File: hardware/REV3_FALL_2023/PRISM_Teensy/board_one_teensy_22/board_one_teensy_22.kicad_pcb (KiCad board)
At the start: 2 copper layers, 61 x 88.9 mm, 21 parts, among them J1 EAST, J2 CORE_IO, J3 USB_micro, U1 Teensy4.1, U2 BNO055_Breakout, U3 3966

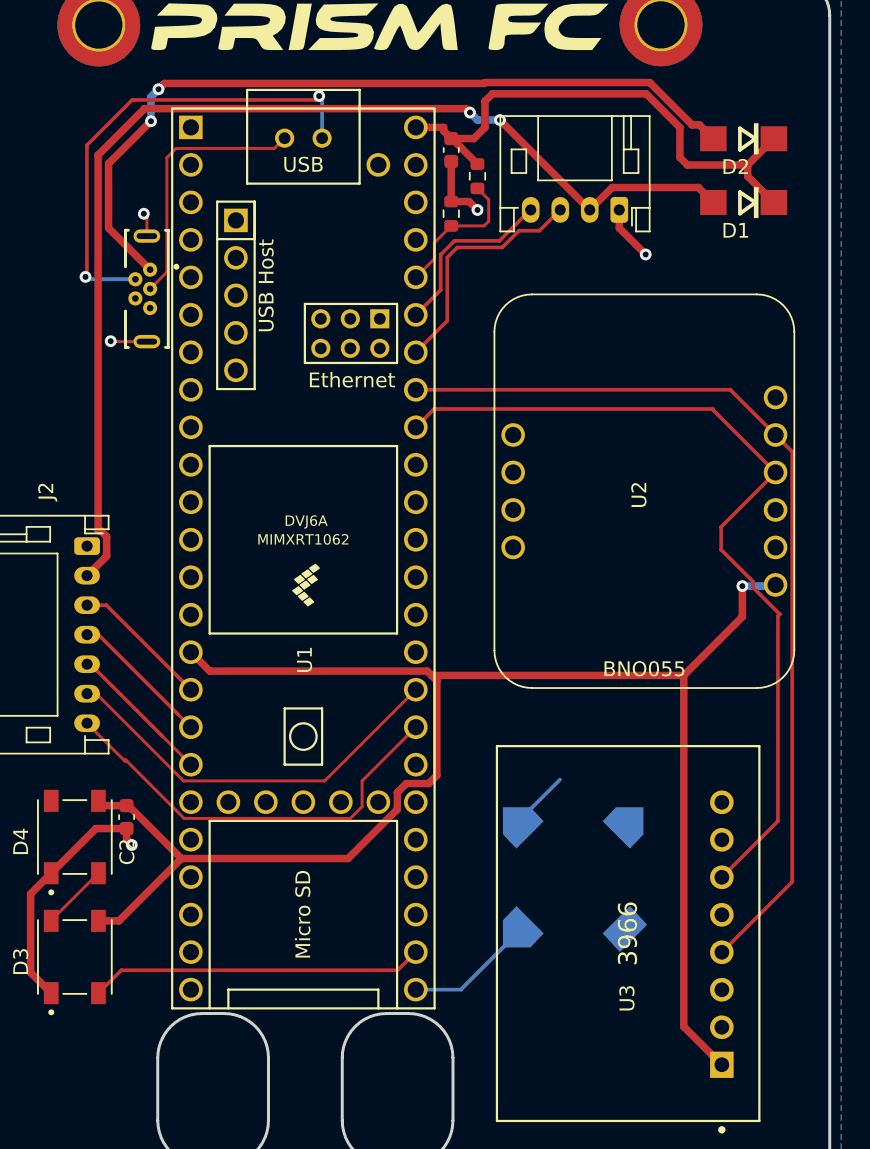
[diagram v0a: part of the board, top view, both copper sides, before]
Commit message: added teensy 4.0 and new connector spec
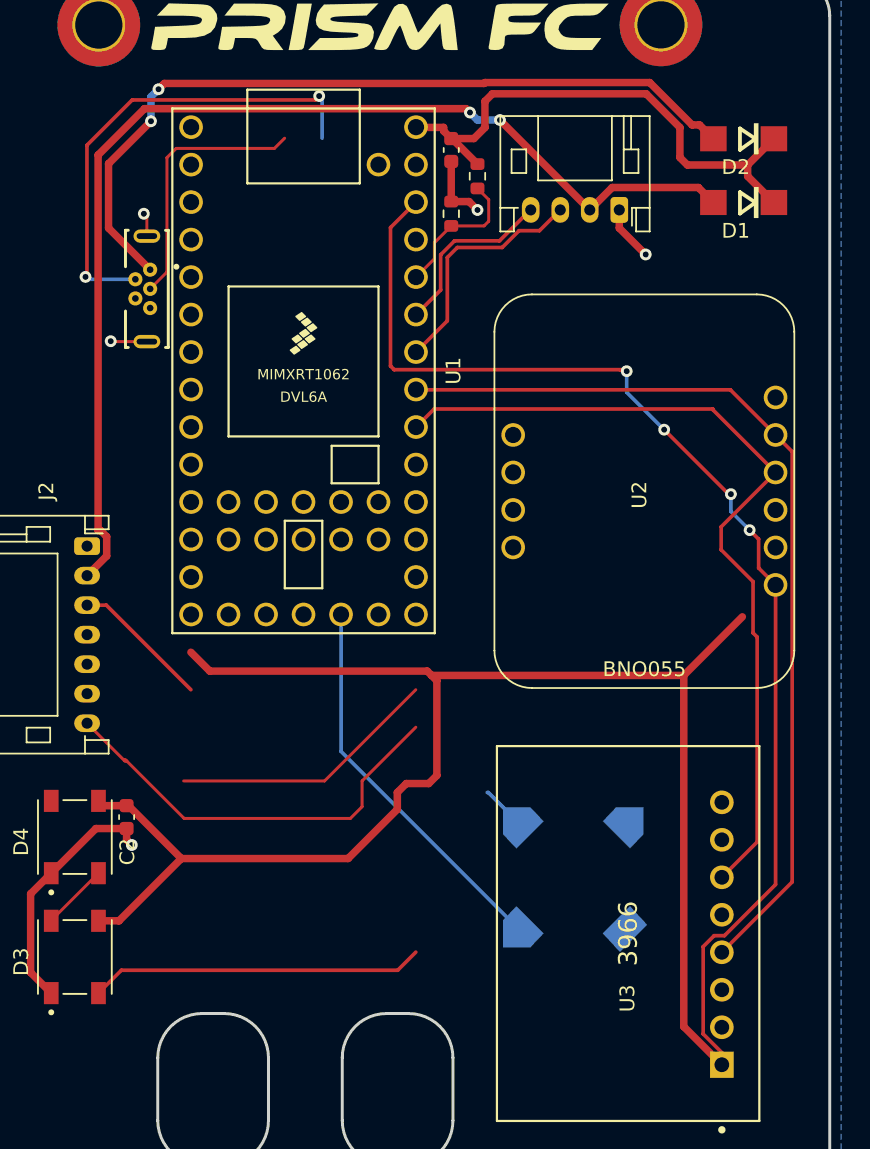
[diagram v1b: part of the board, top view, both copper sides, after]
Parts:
- U1: value Teensy4.1 -> Teensy4.0; footprint Teensy:Teensy41 -> Teensy_4.1:Teensy40
- moved U1 12.7 mm to (132.5, 76.7)
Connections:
- C2 pad 2: /3.3V -> /5V
- D3 pad 3: /3.3V -> /5V
- D4 pad 3: /3.3V -> /5V
- U1 pad 15: /3.3V -> unconnected-(U1-Pad15)
- U1 pad 16: /PYRO 1 -> unconnected-(U1-Pad16)
- U1 pad 17: /PYRO 2 -> unconnected-(U1-Pad17)
- U1 pad 18: /ARM -> /BUZZER
- U1 pad 25: /BUZZER -> /SDA 0
- U1 pad 26: /NEOPIXEL -> /SCL 0
- U1 pad 27: unconnected-(U1-Pad27) -> /CONT 1
- U1 pad 28: unconnected-(U1-Pad28) -> /CONT 2
- U1 pad 31: unconnected-(U1-Pad31) -> /3.3V
- U1 pad 32: /CONT 2 -> GND
- U1 pad 33: /CONT 1 -> /5V
- U1 pad 35: unconnected-(U1-Pad35) -> /PYRO 1
- U1 pad 36: unconnected-(U1-Pad36) -> /PYRO 2
- U1 pad 37: unconnected-(U1-Pad37) -> /ARM
- U1 pad 38: unconnected-(U1-Pad38) -> /V_SENSE
- U1 pad 40: /SDA 0 -> unconnected-(U1-Pad40)
- U1 pad 41: /SCL 0 -> unconnected-(U1-Pad41)
- U1 pad 42: /TX 0 -> unconnected-(U1-Pad42)
- U1 pad 43: /RX 0 -> unconnected-(U1-Pad43)
- U1 pad 44: Net-(R4-Pad2) -> unconnected-(U1-Pad44)
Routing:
- net /5V: track 0.00 -> 108.9 mm
- net /3.3V: track 113.3 -> 82.1 mm, vias 1 -> 4
- net /BUZZER: track 8.72 -> 26.4 mm
- net /TX 0: track 16.3 -> 0.00 mm
- net /RX 0: track 12.1 -> 0.00 mm
- net /CONT 2: track 28.7 -> 40.8 mm
- net /ARM: track 9.86 -> 0.23 mm
- net /PYRO 2: track 9.63 -> 0.77 mm
- net /CONT 1: track 27.3 -> 35.2 mm
- net /SDA 0: track 58.9 -> 57.7 mm
- net GND: track 33.7 -> 32.9 mm

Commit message: add led
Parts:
- added J1: DM3CS-SF, DM3:HRS_DM3CS-SF, F.Cu at (97.0, 123.3)
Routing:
- net /5V: track 108.9 -> 0.00 mm
- net /3.3V: track 82.1 -> 191.0 mm
- net /TX 0: track 0.00 -> 16.3 mm
- net /CONT 1: track 35.2 -> 18.9 mm
- net /RX 0: track 0.00 -> 12.1 mm
- net /CONT 2: track 40.8 -> 28.7 mm

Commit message: moving GPS and Radio to main
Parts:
- removed the J1 at (153.9, 65.8)
- removed U2: BNO055_Breakout, Sensors:BNO055_Breakout
- added D5: WS2812B, LED_SMD:LED_WS2812B_PLCC4_5.0x5.0mm_P3.2mm, F.Cu at (179.0, 116.0)
- added J3: 3387, LSM9DS1:3387, F.Cu at (193.6, 87.6)
- moved J1 17.3 mm to (84.8, 111.0)
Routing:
- net /3.3V: track 191.0 -> 0.00 mm, vias 4 -> 0
- net /V_BATT: track 76.3 -> 0.00 mm, vias 2 -> 0
- net /SCL 0: track 63.1 -> 0.00 mm
- net /SDA 0: track 57.7 -> 0.00 mm
- net /V_USB: track 54.2 -> 0.00 mm, vias 2 -> 0
- net /VIN: track 36.7 -> 0.05 mm
- net Net-(J3-Pad2): track 32.5 -> 0.00 mm, vias 2 -> 0
- net GND: track 32.9 -> 3.42 mm, vias 5 -> 0
- net /CONT 2: track 28.7 -> 0.00 mm
- net /BUZZER: track 26.4 -> 0.00 mm
- net /NEOPIXEL: track 22.7 -> 0.00 mm
- net /CONT 1: track 18.9 -> 0.63 mm
- net Net-(J3-Pad3): track 17.9 -> 0.00 mm
- net /TX 0: track 16.3 -> 0.00 mm
- net /RX 0: track 12.1 -> 0.00 mm
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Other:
- board text removed: "Ari Bobesh Charlie Babe Jiayuan Liu Lili Baker Rowan Jansens"

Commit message: Finished Schematic
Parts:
- added C3: C_100nF, footprints:C_0603_1608Metric, F.Cu at (187.2, 124.5)
- added C4: C_100nF, footprints:C_0603_1608Metric, F.Cu at (187.2, 127.0)
- added C5: C_10uF, footprints:C_0805_OEM, F.Cu at (178.0, 129.5)
- added C6: C_100nF, footprints:C_0603_1608Metric, F.Cu at (187.2, 129.5)
- added C7: C_10nF, footprints:C_1206_OEM, F.Cu at (178.5, 121.7)
- added R1: R_10K, footprints:R_0805_OEM, F.Cu at (183.1, 124.7)
- added R2: R_10K, footprints:R_0805_OEM, F.Cu at (183.1, 127.6)
- added R3: R_10K, footprints:R_0805_OEM, F.Cu at (183.1, 130.5)
- added U5: LSM9DS1, Package_LGA:LGA-24L_3x3.5mm_P0.43mm, F.Cu at (178.4, 125.7)
